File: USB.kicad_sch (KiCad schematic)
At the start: 12 parts, among them J6 USB_C_Receptacle_USB2.0_16P, J9 USB_C_Receptacle_USB2.0_16P, U2 USBLC6-2SC6, U4 USBLC6-2SC6

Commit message: Interface Update
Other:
- company: (none) -> Peter Hancak
- title: (none) -> ESP32P4C5_BOARD
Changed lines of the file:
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@@
 	(generator_version "8.0")
 	(paper "A4")
+	(title_block
+		(title "ESP32P4C5_BOARD")
+		(date "2026-06-01")
+		(rev "A")
+		(company "Peter Hancak")
+	)
 	(junction
 		(at 125.73 125.73)

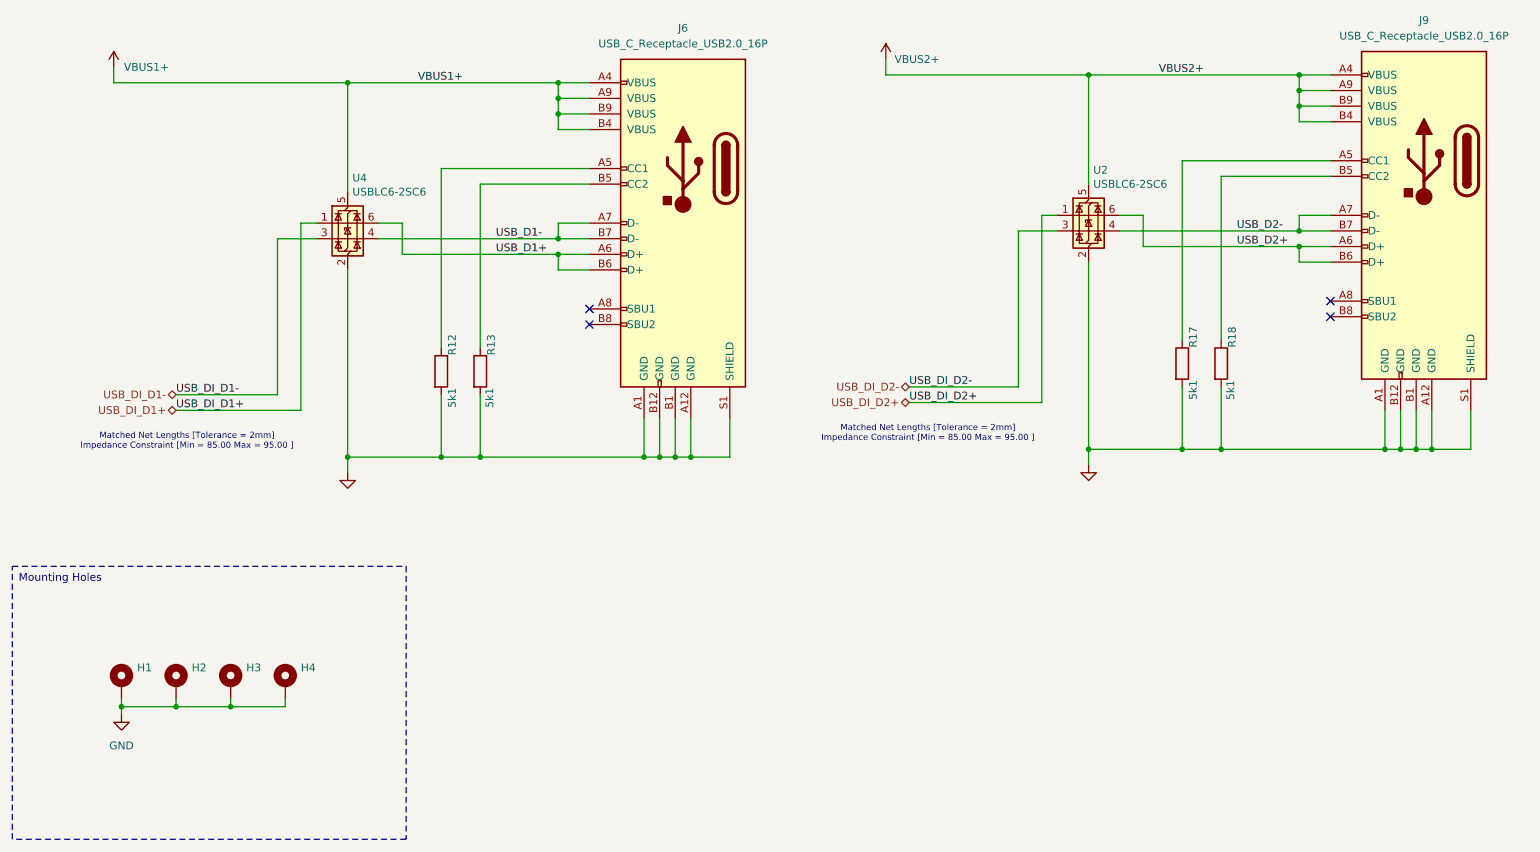
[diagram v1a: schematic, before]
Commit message: Small trace layout fixes
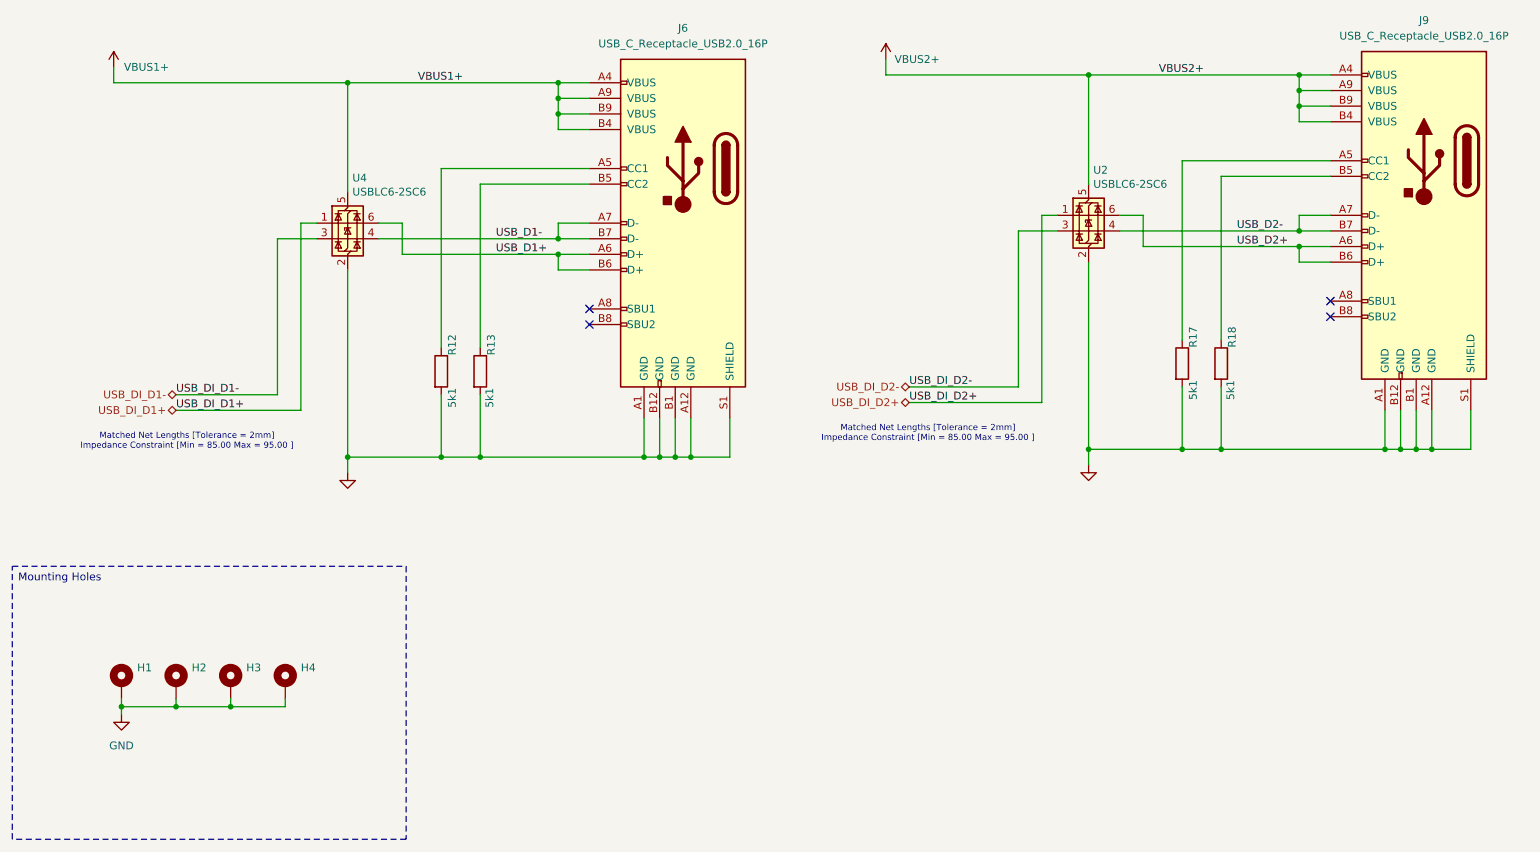
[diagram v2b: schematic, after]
